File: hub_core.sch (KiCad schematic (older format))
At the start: 0 parts

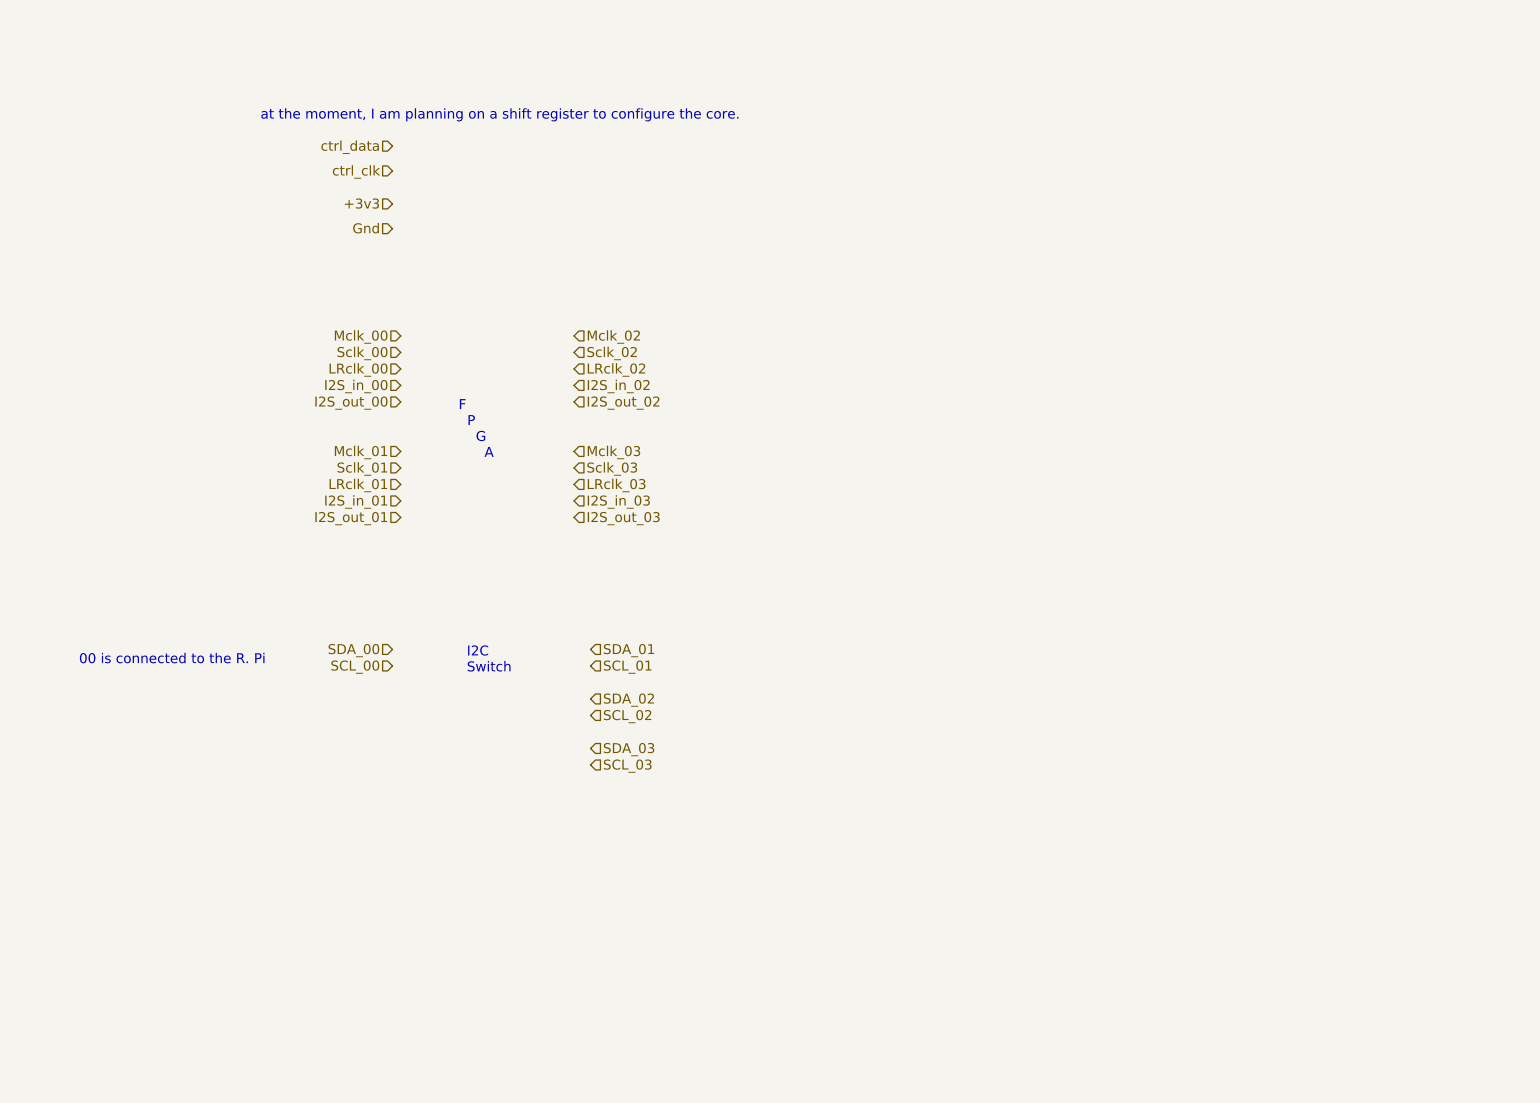
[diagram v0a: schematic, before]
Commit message: preliminary schematic using discrete logic chips
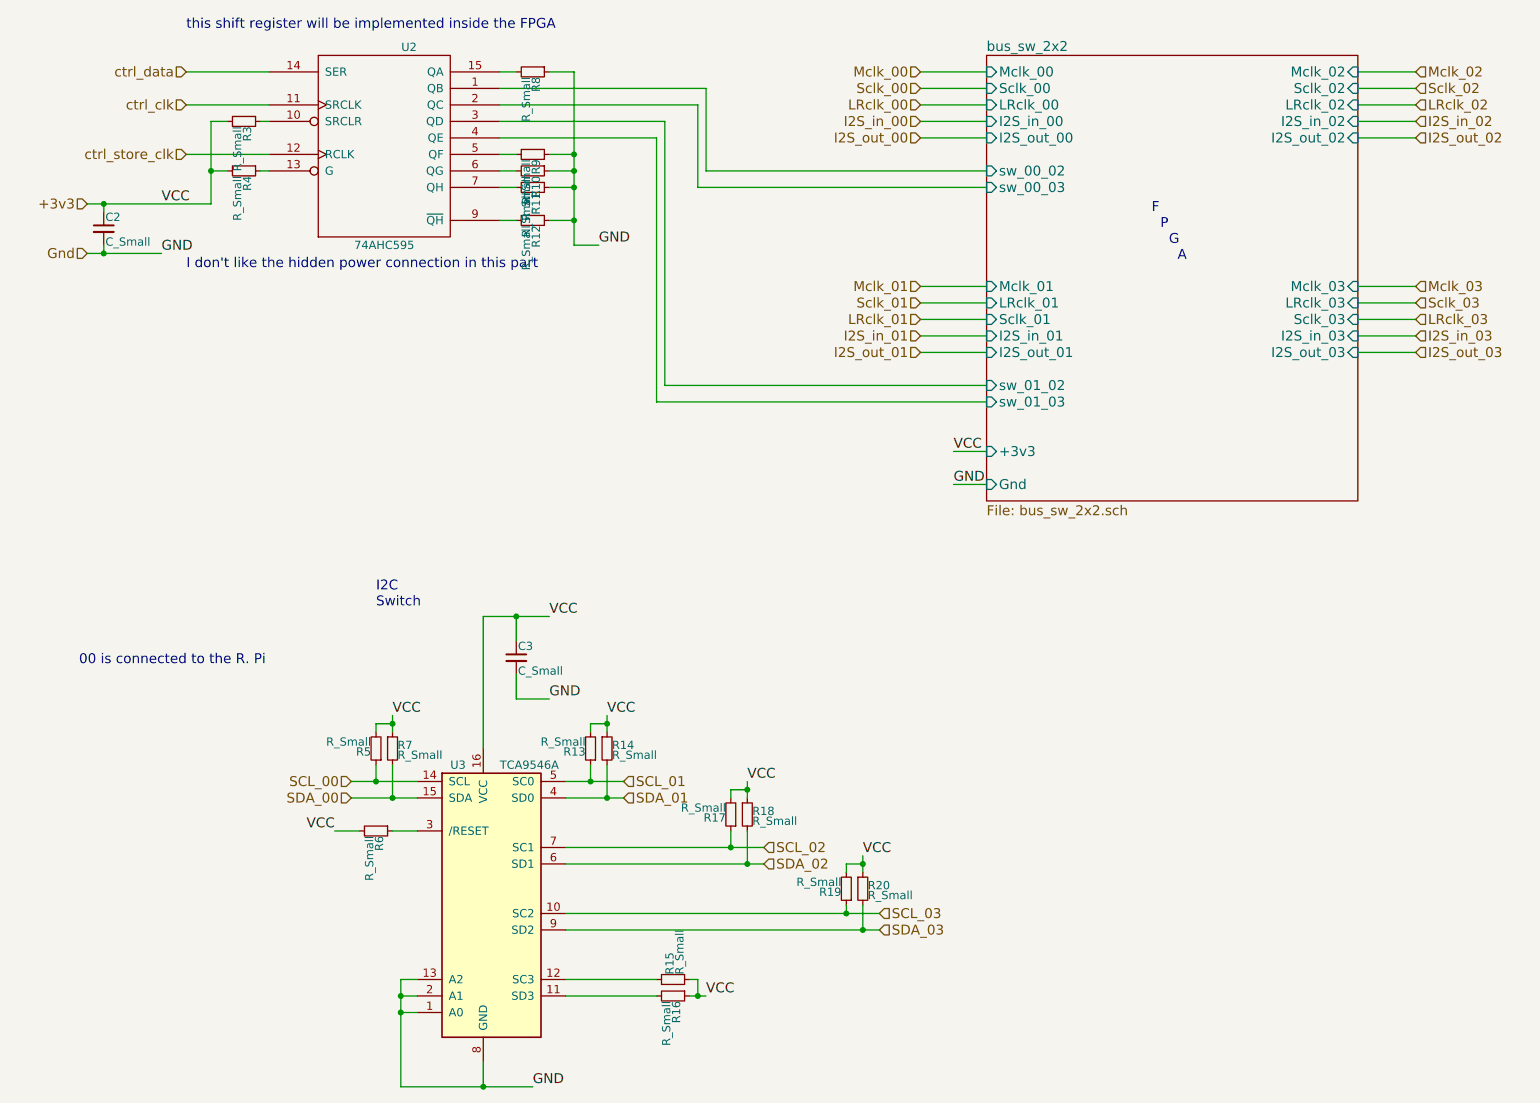
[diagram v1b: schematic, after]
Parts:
- added C2, C3: C_Small, Capacitors_SMD:C_0805_HandSoldering, symbol C_Small
- added R10, R11, R12, R13, R14, R15, R16, R17, R18, R19, R20, R3, R4, R5, R6, R7, R8, R9: R_Small, Resistors_SMD:R_0805_HandSoldering, symbol R_Small
- added U2: 74AHC595, Housings_SOIC:SOIC-16_3.9x9.9mm_Pitch1.27mm, symbol 74HC595
- added U3: TCA9546A, Housings_SSOP:TSSOP-16_4.4x5mm_Pitch0.65mm, symbol TCA9546A
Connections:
- net SCL_00: now also R5.1, U3.14 (SCL)
- net SCL_01: now also R13.1, U3.5 (SC0)
- net SCL_02: now also R17.1, U3.7 (SC1)
- net SCL_03: now also R19.1, U3.10 (SC2)
- net SDA_00: now also R7.2, U3.15 (SDA)
- net SDA_01: now also R14.2, U3.4 (SD0)
- net SDA_02: now also R18.2, U3.6 (SD1)
- net SDA_03: now also R20.2, U3.9 (SD2)
- net ctrl_clk: now also U2.11 (SRCLK)
- net ctrl_data: now also U2.14 (SER)
- new net: R3.1, U2.10 (SRCLR)
- new net: R4.1, U2.13 (G)
- new net: R8.2, U2.15 (QA)
- new net: R9.2, U2.5 (QF)
- new net: R10.2, U2.6 (QG)
- new net: R11.2, U2.7 (QH)
- new net: R12.2, U2.9 (~QH)
- new net: R16.2, U3.11 (SD3)
- new net: R15.1, U3.12 (SC3)
- new net: R6.1, U3.3 (/RESET)
- new net GND: C2.2, C3.2, R10.1, R11.1, R12.1, R8.1, R9.1, U2.8 (GND), U3.1 (A0), U3.13 (A2), U3.2 (A1), U3.8 (GND)
- new net VCC: C2.1, C3.1, R13.2, R14.1, R15.2, R16.1, R17.2, R18.1, R19.2, R20.1, R3.2, R4.2, R5.2, R6.2, R7.1, U2.16 (VCC), U3.16 (VCC)
- new net bus_sw_2x2/sw_00_02: U2.1 (QB)
- new net bus_sw_2x2/sw_00_03: U2.2 (QC)
- new net bus_sw_2x2/sw_01_02: U2.3 (QD)
- new net bus_sw_2x2/sw_01_03: U2.4 (QE)
- new net ctrl_store_clk: U2.12 (RCLK)
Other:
- note added: "I don't like the hidden power connection in this part"
- note added: "this shift register will be implemented inside the FPGA"
- note removed: "at the moment, I am planning on a shift register to configure the core."

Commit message: finished layout
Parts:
- removed R10, R9: R_Small, Resistors_SMD:R_0805_HandSoldering, symbol R_Small
- added C16: C_Small, Capacitors_SMD:C_0805_HandSoldering, symbol C_Small
- added R56: R_Small, Resistors_SMD:R_0805_HandSoldering, symbol R_Small
- added R57, R58: 3k9, Resistors_SMD:R_0805_HandSoldering, symbol R_Small
- added U12: AT24CS32-SSHM, Housings_SOIC:SOIC-8_3.9x4.9mm_Pitch1.27mm, symbol AT24CS32-SSHM
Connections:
- net GND: now also C16.2, U12.2 (A1), U12.3 (A2), U12.4 (GND), U12.7 (WP)
- net SCL_00: now also R58.2, U12.5 (SDA)
- net SDA_00: now also R57.2, U12.6 (SCL)
- net bus_sw_2x2/sw_00_02: now also U2.2 (QC); no longer U2.1 (QB)
- net bus_sw_2x2/sw_00_03: now also U2.3 (QD); no longer U2.2 (QC)
- net bus_sw_2x2/sw_01_02: now also U2.4 (QE); no longer U2.3 (QD)
- net bus_sw_2x2/sw_01_03: now also U2.5 (QF); no longer U2.4 (QE)
- net bus_sw_2x2/sw_02_03: now reaches U2.6 (QG)
- new net: R56.1, U12.1 (A0)
- new net +3V3: C16.1, R56.2, R57.1, R58.1, U12.8 (VCC)
- new net bus_sw_2x2/sw_00_01: U2.1 (QB)
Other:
- note added: "Hub info EEPROM"
- note added: "don't think this\nresistor is needed?"
- moved on the sheet: C2, C3, R13, R14, R15, R16, R17, R18, R19, R20, R5, R6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
